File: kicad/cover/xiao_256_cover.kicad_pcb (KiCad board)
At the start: 2 copper layers, 22 x 96 mm, 4 parts

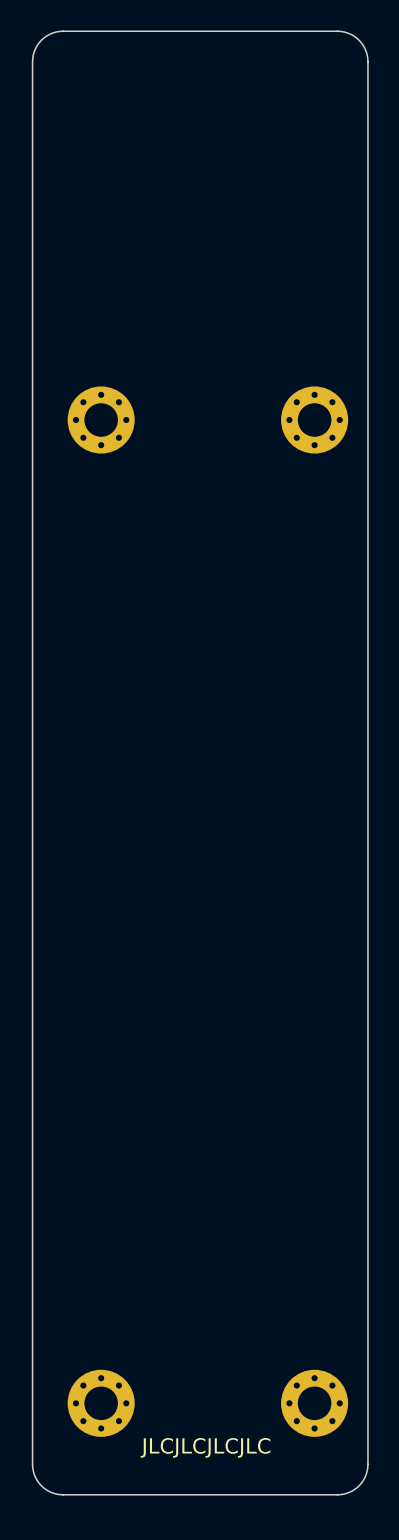
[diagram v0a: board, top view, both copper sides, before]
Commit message: make cover symmetric
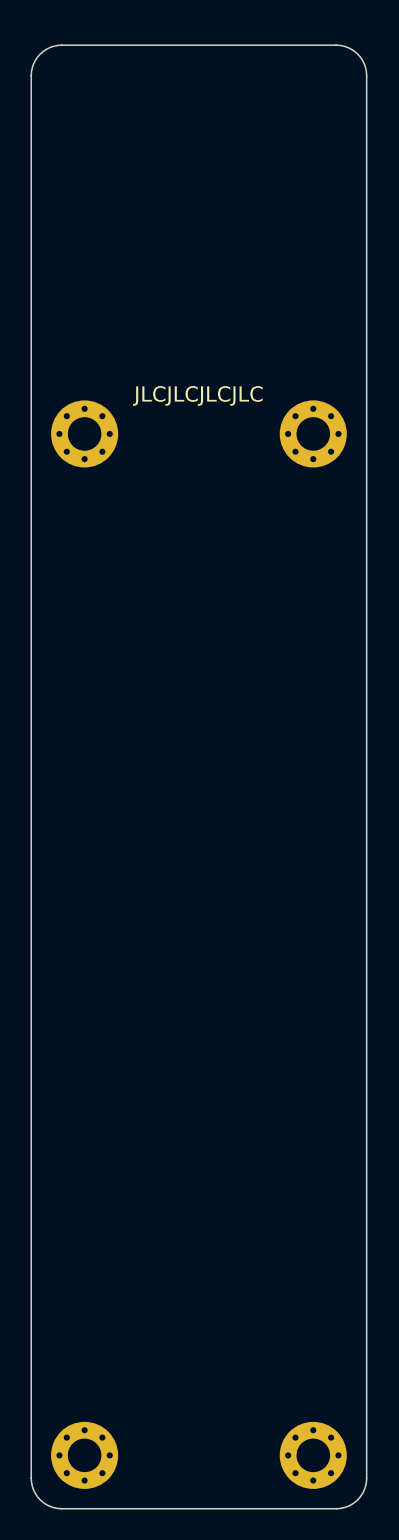
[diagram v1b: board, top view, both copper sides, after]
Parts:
- moved REF** 3.58 mm to (33.5, 107.5)
- moved REF** 3.42 mm to (48.5, 107.5)
- moved REF** 1.42 mm to (33.5, 40.5)
- moved REF** 0.92 mm to (48.5, 40.5)
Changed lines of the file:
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@@
   (net 0 "")
   (footprint "xiao_256:Mount_M2" (layer "F.Cu")
-    (at 48.585786 39.585786)
+    (at 48.5 40.5)
     (descr "Mounting Hole 2.2mm, M2")
     (tags "mounting hole 2.2mm m2")
@@
   )
   (footprint "xiao_256:Mount_M2" (layer "F.Cu")
-    (at 48.585786 104.085786)
+    (at 48.5 107.5)
     (descr "Mounting Hole 2.2mm, M2")
     (tags "mounting hole 2.2mm m2")
@@
   )
   (footprint "xiao_256:Mount_M2" (layer "F.Cu")
-    (at 34.585786 39.585786)
+    (at 33.5 40.5)
     (descr "Mounting Hole 2.2mm, M2")
     (tags "mounting hole 2.2mm m2")
@@
   )
   (footprint "xiao_256:Mount_M2" (layer "F.Cu")
-    (at 34.585786 104.085786)
+    (at 33.5 107.5)
     (descr "Mounting Hole 2.2mm, M2")
     (tags "mounting hole 2.2mm m2")
@@
     (pad "1" thru_hole circle (at 1.65 0) (size 0.7 0.7) (drill 0.4) (layers "*.Cu" "*.Mask"))
   )
-  (gr_arc (start 32.085786 110.085786) (mid 30.671572 109.5) (end 30.085786 108.085786)
+  (gr_arc (start 32 111) (mid 30.5858 110.414208) (end 30 109)
     (stroke (width 0.1) (type default)) (layer "Edge.Cuts"))
-  (gr_line (start 32.085786 14.085786) (end 50.085786 14.085786)
+  (gr_line (start 32 15) (end 50 15)
     (stroke (width 0.1) (type default)) (layer "Edge.Cuts"))
-  (gr_line (start 30.085786 108.085786) (end 30.085786 16.085786)
+  (gr_line (start 30 109) (end 30 17)
     (stroke (width 0.1) (type default)) (layer "Edge.Cuts"))
-  (gr_arc (start 52.085786 108.085786) (mid 51.5 109.5) (end 50.085786 110.085786)
+  (gr_arc (start 52 109) (mid 51.414218 110.414218) (end 50 111)
     (stroke (width 0.1) (type default)) (layer "Edge.Cuts"))
-  (gr_line (start 52.085786 16.085786) (end 52.085786 108.085786)
+  (gr_line (start 52 17) (end 52 109)
     (stroke (width 0.1) (type default)) (layer "Edge.Cuts"))
-  (gr_arc (start 30.085786 16.085786) (mid 30.671572 14.671572) (end 32.085786 14.085786)
+  (gr_arc (start 30 17) (mid 30.585791 15.585791) (end 32 15)
     (stroke (width 0.1) (type default)) (layer "Edge.Cuts"))
-  (gr_arc (start 50.085786 14.085786) (mid 51.5 14.671572) (end 52.085786 16.085786)
+  (gr_arc (start 50 15) (mid 51.414228 15.585781) (end 52 17)
     (stroke (width 0.1) (type default)) (layer "Edge.Cuts"))
-  (gr_line (start 50.085786 110.085786) (end 32.085786 110.085786)
+  (gr_line (start 50 111) (end 32 111)
     (stroke (width 0.1) (type default)) (layer "Edge.Cuts"))
-  (gr_text "JLCJLCJLCJLC" (at 41.5 107.5) (layer "F.SilkS")
+  (gr_text "JLCJLCJLCJLC" (at 41 38.5) (layer "F.SilkS")
     (effects (font (size 1 1) (thickness 0.15)) (justify bottom))
   )
